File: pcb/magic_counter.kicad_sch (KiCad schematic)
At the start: 8 parts, among them J1 ISP-Port, U1 ATmega32A-P, Y1 Crystal

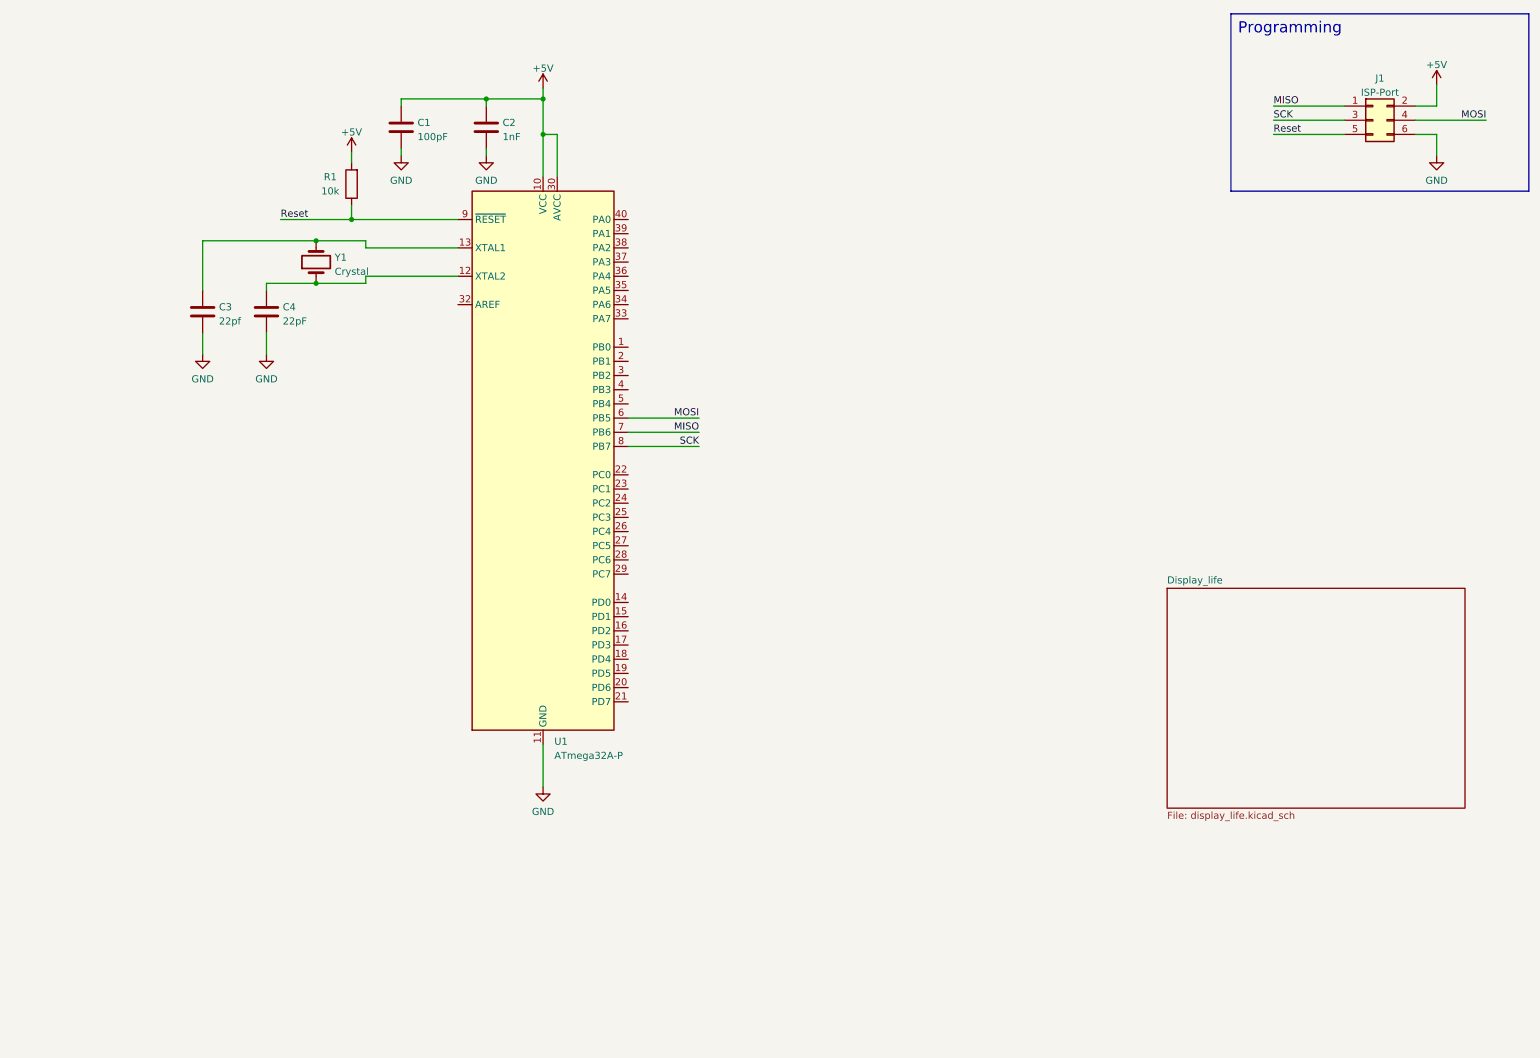
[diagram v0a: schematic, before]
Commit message: test layout and first traces
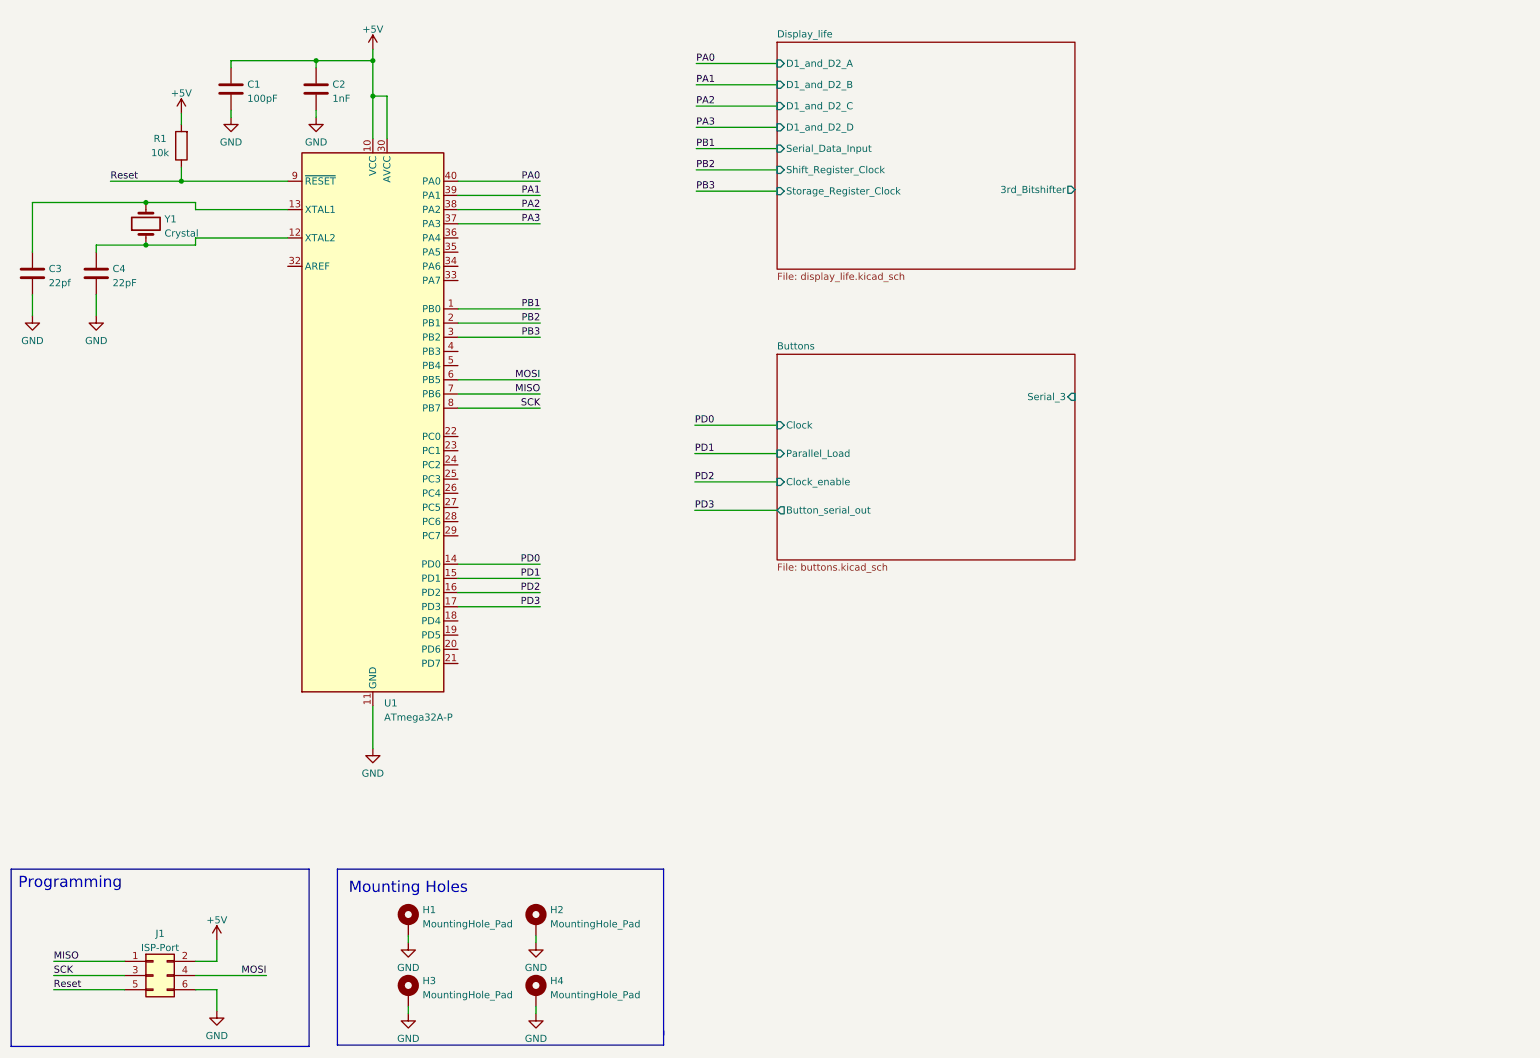
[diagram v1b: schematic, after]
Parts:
- added H1, H2, H3, H4: MountingHole_Pad, MountingHole:MountingHole_3.2mm_M3_DIN965_Pad, symbol Mechanical:MountingHole_Pad
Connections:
- net GND: now also H1.1, H2.1, H3.1, H4.1
- net PB1: now reaches U1.1 (PB0)
- net PD0: now reaches U1.14 (PD0)
- net PD1: now reaches U1.15 (PD1)
- net PD2: now reaches U1.16 (PD2)
- net PD3: now reaches U1.17 (PD3)
- net PB2: now reaches U1.2 (PB1)
- net PB3: now reaches U1.3 (PB2)
- net PA3: now reaches U1.37 (PA3)
- net PA2: now reaches U1.38 (PA2)
- net PA1: now reaches U1.39 (PA1)
- net PA0: now reaches U1.40 (PA0)
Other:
- added sheet Buttons (buttons.kicad_sch)
- sheet Display_life ports: added 3rd_Bitshifter, D1_and_D2_A, D1_and_D2_B, D1_and_D2_C, D1_and_D2_D, Serial_Data_Input, Shift_Register_Clock, Storage_Register_Clock; removed none
- note added: "Mounting Holes"
- moved on the sheet: C1, C2, C3, C4, J1, R1, U1, Y1

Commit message: new layout test
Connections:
- net PA7: now reaches U1.33 (PA7)
- net PA6: now reaches U1.34 (PA6)
- net PA5: now reaches U1.35 (PA5)
- net PA4: now reaches U1.36 (PA4)
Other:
- sheet Buttons renamed Buttons_Row_1_and_2
- added sheet Buttons_Row_3_and_4 (buttons_3_4.kicad_sch)
- added sheet Display_3_and_4 (Display_3_and_4.kicad_sch)
- sheet Buttons_Row_1_and_2: file buttons.kicad_sch -> buttons_1_2.kicad_sch

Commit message: datasheets added
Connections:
- net PB3 is gone; now on net PB2: U1.3 (PB2)
- net PB1: now also U1.2 (PB1); no longer U1.1 (PB0)
- net PB2: no longer U1.2 (PB1)
- new net PB0: U1.1 (PB0)
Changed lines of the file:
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@@
     (effects (font (size 1.27 1.27)) (justify left bottom))
   )
-  (label "PB3" (at 120.142 96.52 0)
+  (label "PB2" (at 120.142 96.52 0)
     (effects (font (size 1.27 1.27)) (justify left bottom))
   )
-  (label "PB1" (at 120.142 34.036 0)
+  (label "PB0" (at 120.142 34.036 0)
     (effects (font (size 1.27 1.27)) (justify left bottom))
   )
@@
     (effects (font (size 1.27 1.27)) (justify right bottom))
   )
-  (label "PB2" (at 120.142 37.846 0)
+  (label "PB1" (at 120.142 37.846 0)
     (effects (font (size 1.27 1.27)) (justify left bottom))
   )
@@
     (effects (font (size 1.27 1.27)) (justify left bottom))
   )
-  (label "PB3" (at 120.142 41.656 0)
+  (label "PB2" (at 120.142 41.656 0)
     (effects (font (size 1.27 1.27)) (justify left bottom))
   )
-  (label "PB3" (at 107.442 70.612 180)
+  (label "PB2" (at 107.442 70.612 180)
     (effects (font (size 1.27 1.27)) (justify right bottom))
   )
@@
     (effects (font (size 1.27 1.27)) (justify right bottom))
   )
-  (label "PB1" (at 107.442 65.532 180)
+  (label "PB0" (at 107.442 65.532 180)
     (effects (font (size 1.27 1.27)) (justify right bottom))
   )
@@
     (effects (font (size 1.27 1.27)) (justify right bottom))
   )
-  (label "PB2" (at 120.142 91.44 0)
+  (label "PB1" (at 120.142 91.44 0)
     (effects (font (size 1.27 1.27)) (justify left bottom))
   )
@@
     (effects (font (size 1.27 1.27)) (justify right bottom))
   )
-  (label "PB2" (at 107.442 68.072 180)
+  (label "PB1" (at 107.442 68.072 180)
     (effects (font (size 1.27 1.27)) (justify right bottom))
   )

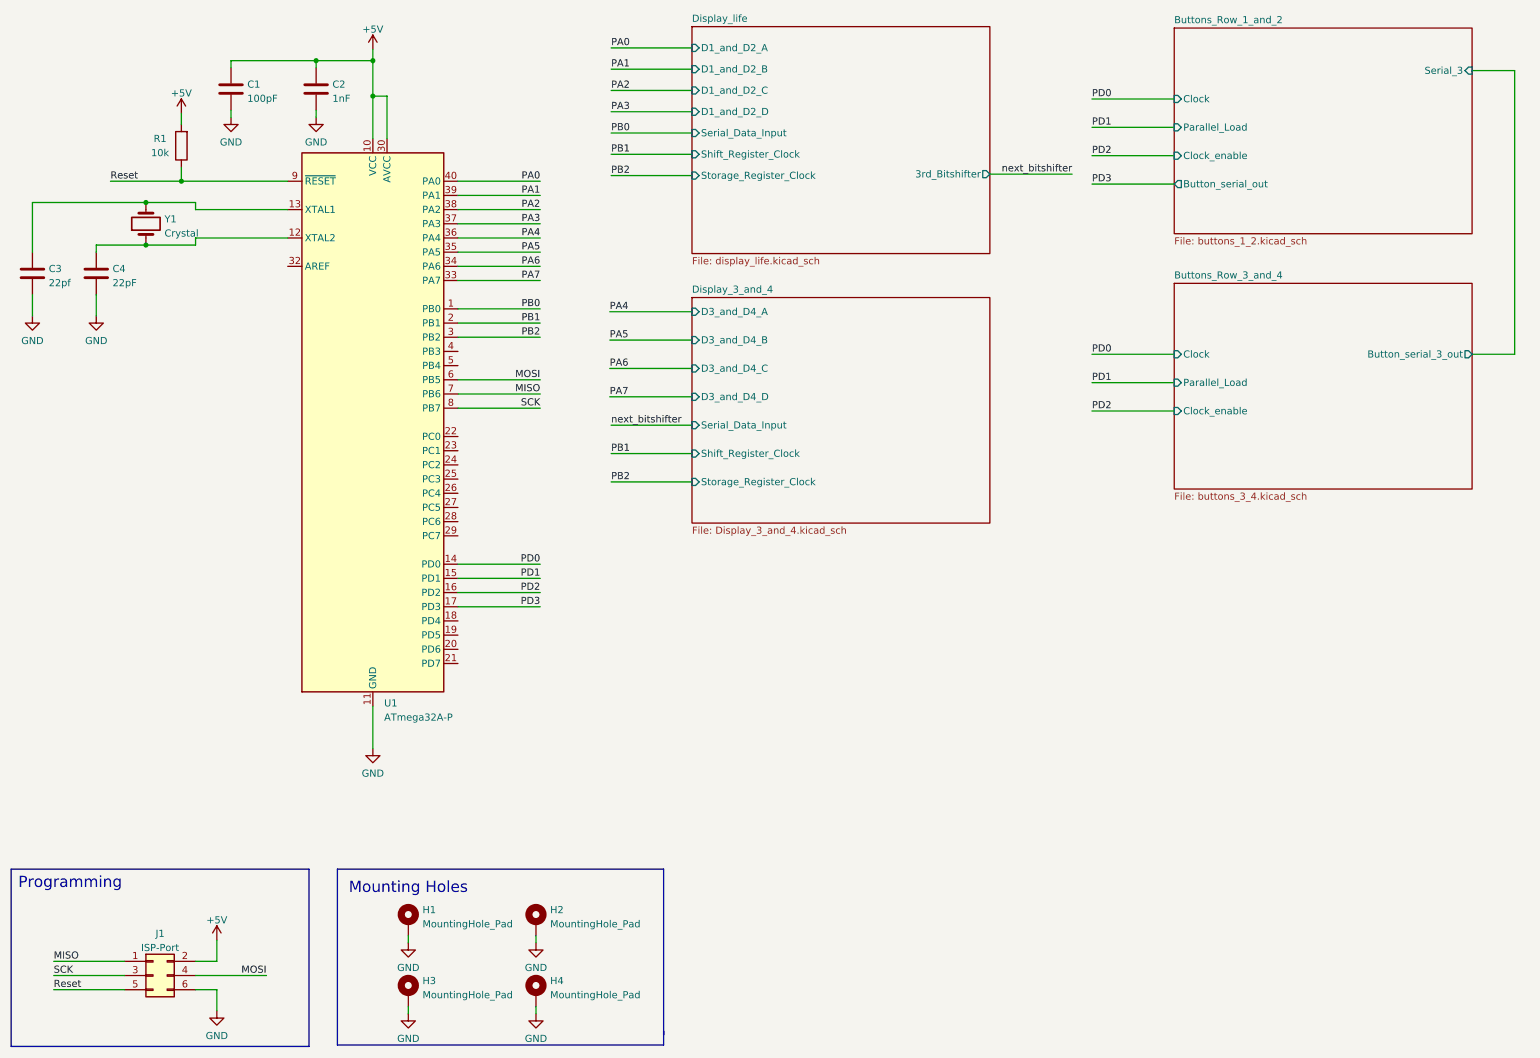
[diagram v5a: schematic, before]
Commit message: fewer parts and reduced to prototyping board with more logic analyzer pins
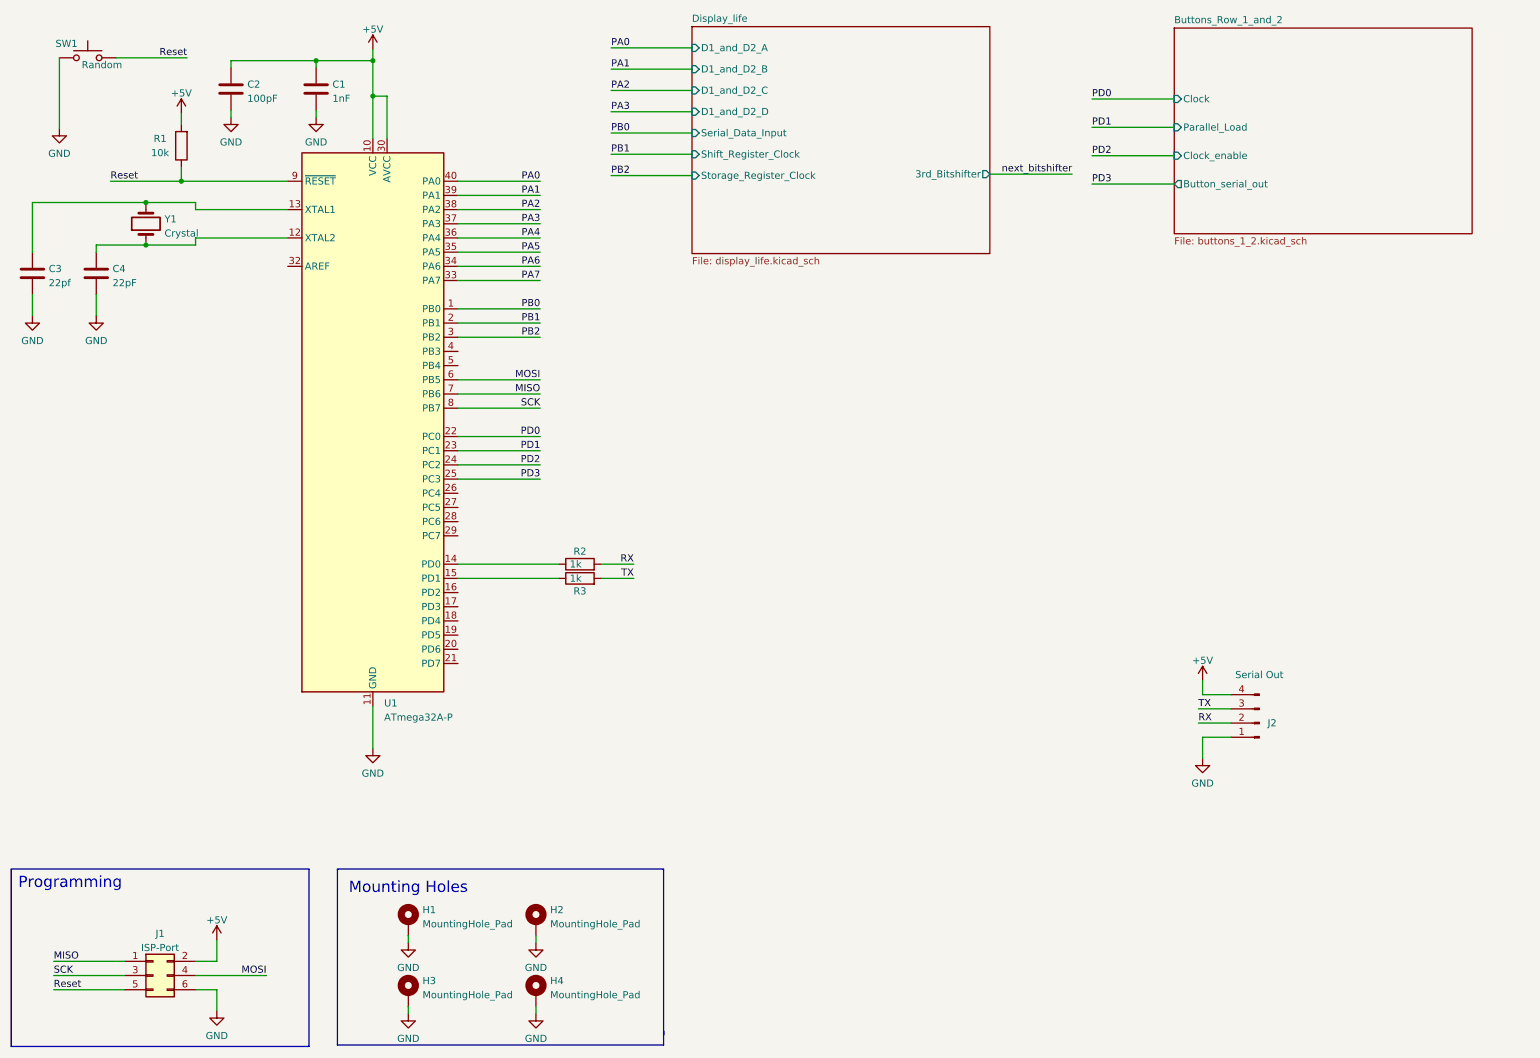
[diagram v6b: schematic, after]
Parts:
- added J2: Serial Out, Connector_PinHeader_2.54mm:PinHeader_1x04_P2.54mm_Vertical, symbol Connector:Conn_01x04_Male
- added R2, R3: 1k, Resistor_THT:R_Axial_DIN0207_L6.3mm_D2.5mm_P7.62mm_Horizontal, symbol Device:R
- added SW1: Random, Button_Switch_THT:SW_PUSH_6mm_H5mm, symbol Switch:SW_Push
- renumbered C2 to C1, C1 to C2
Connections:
- net +5V: now also J2.4 (Pin_4)
- net GND: now also J2.1 (Pin_1), SW1.1
- net PD0: now also U1.22 (PC0); no longer U1.14 (PD0)
- net PD1: now also U1.23 (PC1); no longer U1.15 (PD1)
- net PD2: now also U1.24 (PC2); no longer U1.16 (PD2)
- net PD3: now also U1.25 (PC3); no longer U1.17 (PD3)
- net Reset: now also SW1.2
- new net: R3.1, U1.15 (PD1)
- new net: R2.1, U1.14 (PD0)
- new net RX: J2.2 (Pin_2), R2.2
- new net TX: J2.3 (Pin_3), R3.2
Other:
- removed sheet Buttons_Row_3_and_4
- removed sheet Display_3_and_4
- sheet Buttons_Row_1_and_2 ports: added none; removed Serial_3

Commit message: test 1
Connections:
- net PD0 renamed PC0
- net PD1 renamed PC1
- net PD2 renamed PC2
- net PD3 renamed PC3
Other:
- sheet Display_life ports: added none; removed 3rd_Bitshifter
